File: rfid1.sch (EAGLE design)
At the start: 71 parts, among them IC1 EM4095, J1 AVR_SPI_PRG_6PTH, U1 MCP73831, U2 TPS61200, X2 USB-MICROB, Y2 RESONATORSMD

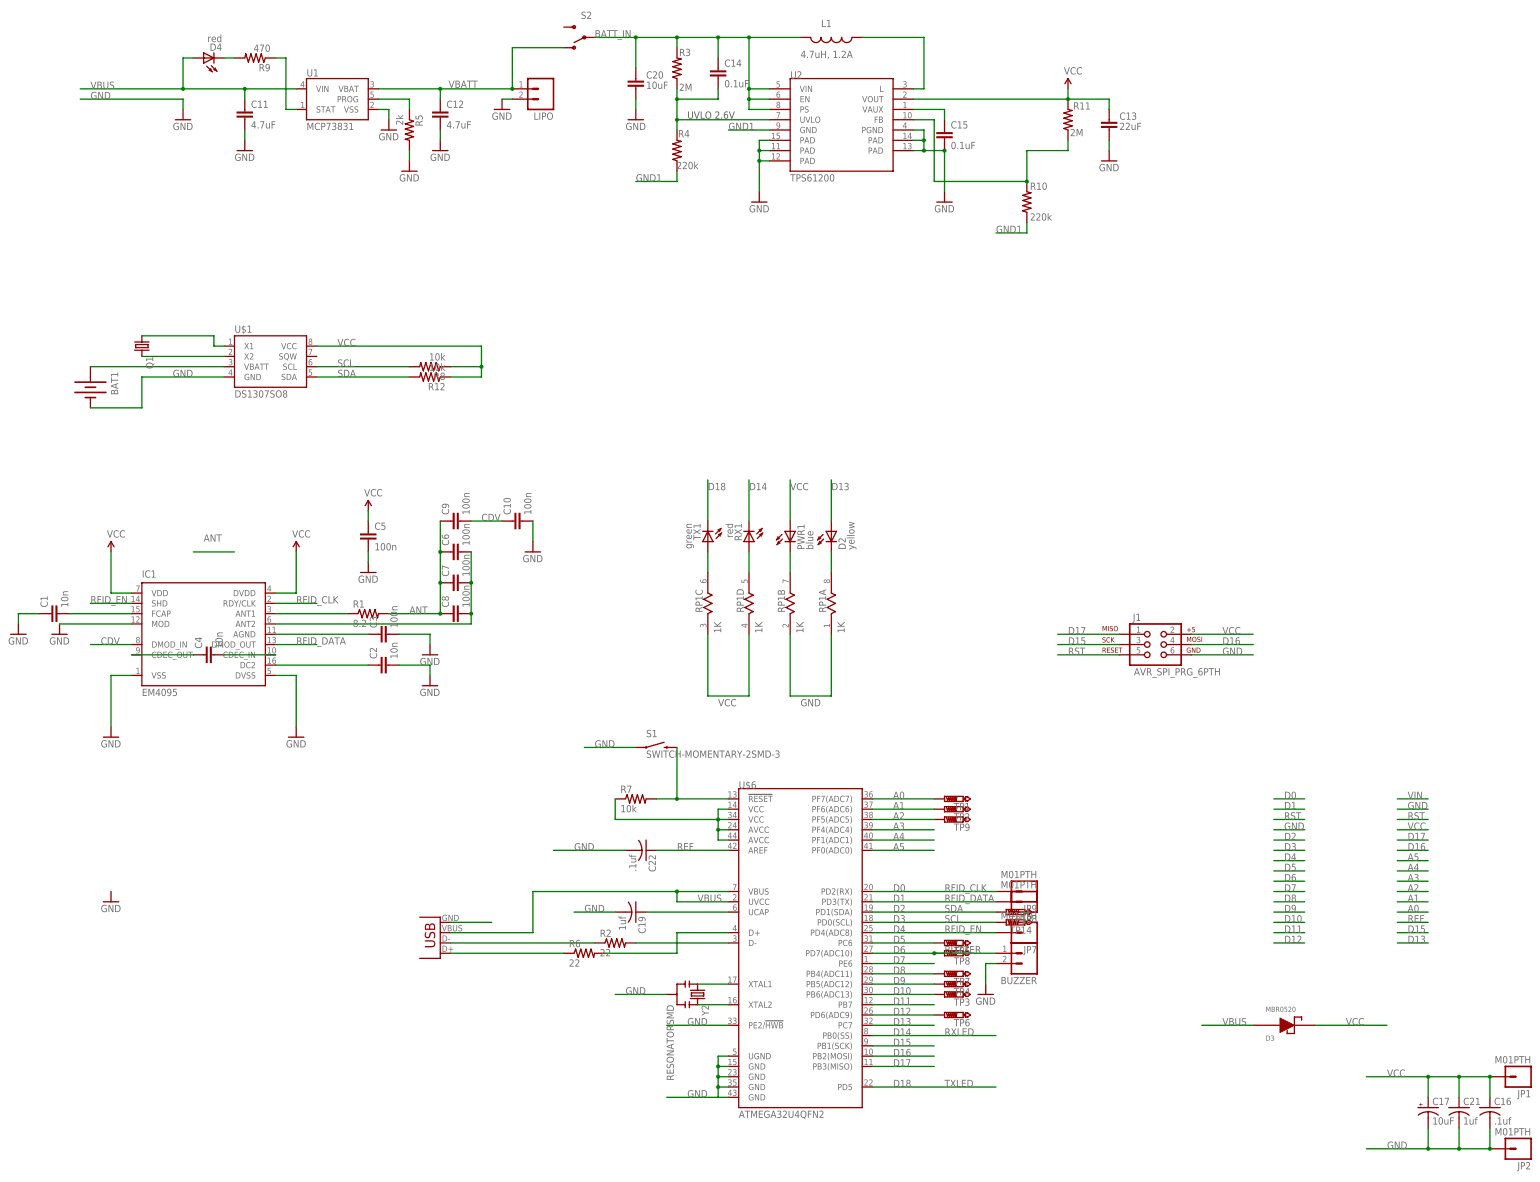
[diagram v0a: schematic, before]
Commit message: Updated part sizes and added acces pads for unused avr pins.  Added silk labels and free area.  Revision sent for manufacturing 6/4/12
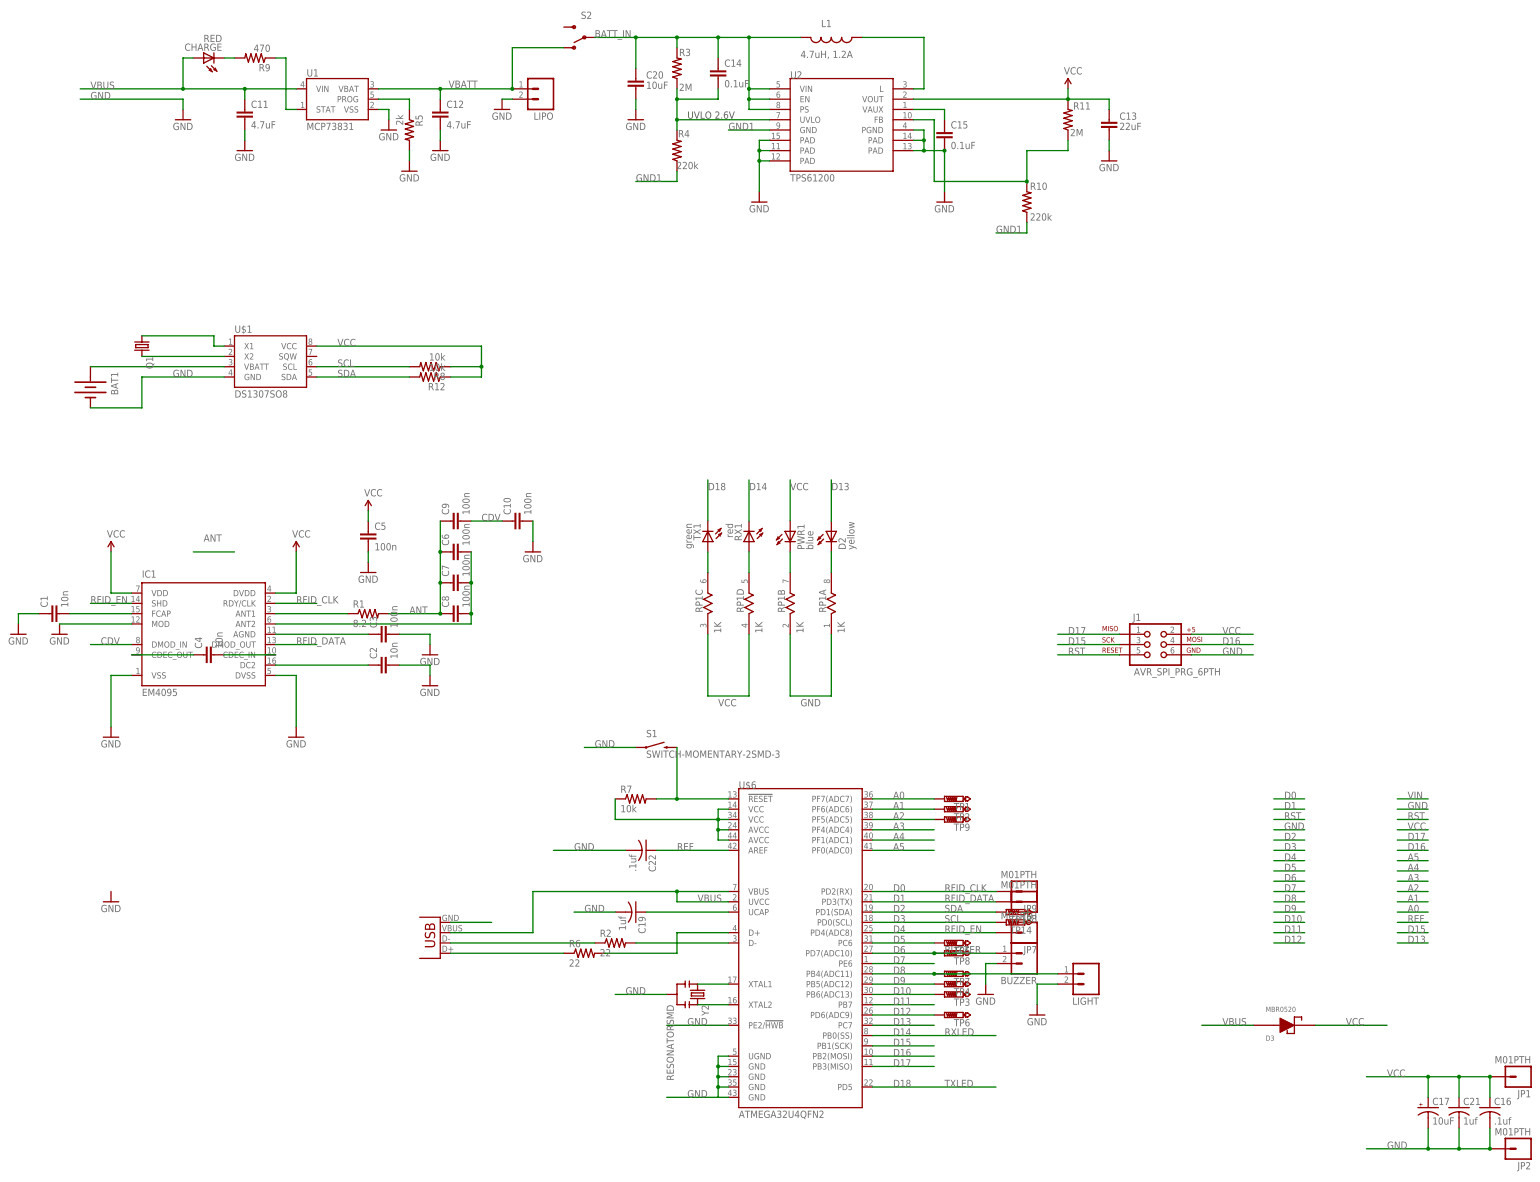
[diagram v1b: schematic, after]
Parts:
- removed D4: red, SparkFun:LED0603
- added CHARGE: RED, led:LEDCHIPLED_0805
- added LIGHT: (no value), SparkFun-Connectors:M02PTH
- C11, C12, C14, C15: device SparkFun:CAP0402-CAP -> SparkFun:CAP0603-CAP
- LIPO: device SparkFun-Connectors:M02PTH -> SparkFun-Connectors:M02-JST-2-PTH-NO_SILK
- R10, R11, R3, R4, R5, R9: device SparkFun:RESISTOR0402-RES -> SparkFun:RESISTOR0603-RES
- TP1, TP13, TP14, TP2, TP3, TP4, TP5, TP6, TP7, TP8, TP9: value PTR1TP15R -> PTR1TP14R; device testpad:PTR1TP15R -> testpad:PTR1TP14R
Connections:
- net D8: now also LIGHT.1
- net GND: now also LIGHT.2
- net N$2: now also CHARGE.C; no longer D4.C
- net VBUS: now also CHARGE.A; no longer D4.A
